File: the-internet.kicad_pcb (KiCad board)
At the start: 2 copper layers, 88 x 40 mm, 12 parts, among them J1 POWER, J2 LOLIN-C3-MINI (L), J3 LOLIN-C3-MINI (R), Q1 KSC1815YTA

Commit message: Maximise space for meme text
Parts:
- turned LS1 to 45 degrees
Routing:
- net +3.3V: track 64.6 -> 70.5 mm
- net Net-(Q1-C): track 68.3 -> 71.3 mm
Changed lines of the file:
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@@
 	(footprint "the-internet:PS1720P02"
 		(layer "F.Cu")
-		(at 77.47 45.4)
+		(at 77.47 45.4 45)
 		(property "Reference" "LS1"
-			(at 0 -9.652 0)
+			(at 0 -9.652 45)
 			(unlocked yes)
 			(layer "F.SilkS")
@@
 		)
 		(property "Value" "PS1720P02"
-			(at 0 1 0)
+			(at 0 1 45)
 			(unlocked yes)
 			(layer "F.Fab")
@@
 		)
 		(property "Datasheet" "https://product.tdk.com/en/system/files/dam/doc/product/sw_piezo/sw_piezo/piezo-buzzer/catalog/piezoelectronic_buzzer_ps_en.pdf"
-			(at 0 0 0)
+			(at 0 0 45)
 			(unlocked yes)
 			(layer "F.Fab")
@@
 		)
 		(property "Description" "Crystal speaker/transducer"
-			(at 0 0 0)
+			(at 0 0 45)
 			(unlocked yes)
 			(layer "F.Fab")
@@
 		(fp_circle
 			(center 0 0)
-			(end 8.5 0)
+			(end 8.500001 0)
 			(stroke
 				(width 0.1)
@@
 		)
 		(fp_text user "${REFERENCE}"
-			(at 0 2.5 0)
+			(at 0 2.5 45)
 			(unlocked yes)
 			(layer "F.Fab")
@@
 		)
 		(pad "1" thru_hole circle
-			(at -5 0)
+			(at -5 0 45)
 			(size 1.4 1.4)
 			(drill 0.9)
@@
 		)
 		(pad "2" thru_hole circle
-			(at 5 0)
+			(at 5 0 45)
 			(size 1.4 1.4)
 			(drill 0.9)
@@
 	)
 	(gr_text "2018\n2019\n2020\n2021\n2022\n2023\n2024"
-		(at 60.96 38.1 0)
+		(at 63.754 38.1 0)
 		(layer "B.SilkS")
 		(effects
@@
 	)
 	(gr_text "September X, 1993\nDas gibt's doch gar nicht\n{dblquote}Toddler with Diaper{dblquote} Model #5653\nIt's over 9000!\nHampster Dance\nAll your base are belong to us\nUwU\nYou're The Man Now, Dog!\nEvery time you masturbate... God kills a kitten\nBadger Badger Badger\nYou Wouldn't Steal a Car\nChuck Norris can divide by zero\nDownfall\nNever Gonna Give You Up\nLoss     | || || |_\nAll Star (Shrek)\nPogChamp\nNyan Cat\nIs This a Pigeon?\nDoge     wow   very silkscreen\nPress F to pay respects\nBe like Bill\nThis is fine\nDistracted boyfriend"
-		(at 105.537 26.289 0)
+		(at 105.664 26.289 0)
 		(layer "B.SilkS")
 		(effects
@@
 	)
 	(gr_text "Galaxy Brain\nSir, this is a Wendy's\nSoyjaks vs. Chads\namogus (sus)\nGirl Explaining\nYou Like Kissing Boys Don't You\nA Circle?? In the Triangle Factory??"
-		(at 60.452 38.1 0)
+		(at 63.246 38.1 0)
 		(layer "B.SilkS")
 		(effects
@@
 			(keep_text_aligned yes)
 		)
-		(gr_text "88 mm"
+		(gr_text "3464.5669 mils"
 			(at 69.4 69.97 0)
 			(layer "Cmts.User")
@@
 			(keep_text_aligned yes)
 		)
-		(gr_text "5.08"
+		(gr_text "200"
 			(at 19.17 62.865 90)
 			(layer "Cmts.User")
@@
 	)
 	(segment
+		(start 66.675 33.02)
+		(end 61.595 33.02)
+		(width 0.2)
+		(layer "B.Cu")
+		(net 2)
+	)
+	(segment
+		(start 68.58 34.925)
+		(end 66.675 33.02)
+		(width 0.2)
+		(layer "B.Cu")
+		(net 2)
+	)
+	(segment
+		(start 72.430534 48.935534)
+		(end 68.58 45.085)
+		(width 0.2)
+		(layer "B.Cu")
+		(net 2)
+	)
+	(segment
+		(start 73.934466 48.935534)
+		(end 72.430534 48.935534)
+		(width 0.2)
+		(layer "B.Cu")
+		(net 2)
+	)
+	(segment
+		(start 68.58 45.085)
+		(end 68.58 34.925)
+		(width 0.2)
+		(layer "B.Cu")
+		(net 2)
+	)
+	(segment
 		(start 59.055 30.48)
 		(end 54.61 30.48)
@@
 	)
 	(segment
-		(start 68.895 45.4)
-		(end 66.04 42.545)
+		(start 61.595 33.02)
+		(end 59.055 30.48)
 		(width 0.2)
 		(layer "B.Cu")
@@
 	)
 	(segment
-		(start 66.04 37.465)
-		(end 59.055 30.48)
-		(width 0.2)
-		(layer "B.Cu")
-		(net 2)
-	)
-	(segment
-		(start 66.04 42.545)
-		(end 66.04 37.465)
-		(width 0.2)
-		(layer "B.Cu")
-		(net 2)
-	)
-	(segment
-		(start 72.47 45.4)
-		(end 68.895 45.4)
-		(width 0.2)
-		(layer "B.Cu")
-		(net 2)
-	)
-	(segment
 		(start 63.405 59.055)
 		(end 63.405 57.055)
@@
 	)
 	(segment
-		(start 82.47 45.4)
-		(end 80.965 45.4)
+		(start 77.47 43.815)
+		(end 79.420534 41.864466)
 		(width 0.2)
 		(layer "B.Cu")
@@
 	)
 	(segment
-		(start 77.47 48.895)
-		(end 77.47 59.055)
+		(start 77.47 59.055)
+		(end 77.47 43.815)
 		(width 0.2)
 		(layer "B.Cu")
@@
 	)
 	(segment
-		(start 80.965 45.4)
-		(end 77.47 48.895)
+		(start 79.420534 41.864466)
+		(end 81.005534 41.864466)
 		(width 0.2)
 		(layer "B.Cu")

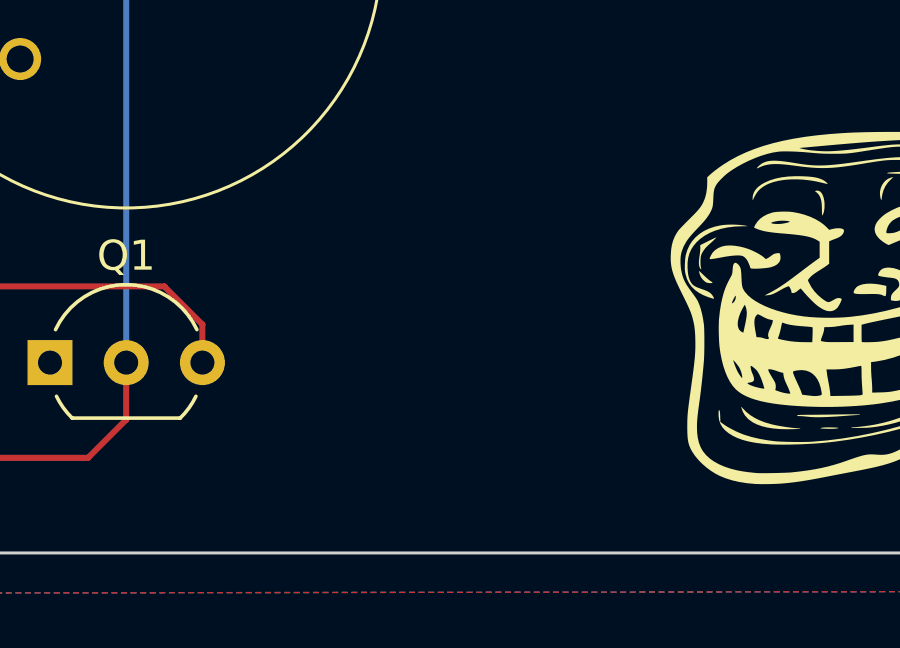
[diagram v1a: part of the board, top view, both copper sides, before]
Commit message: Add square hole game
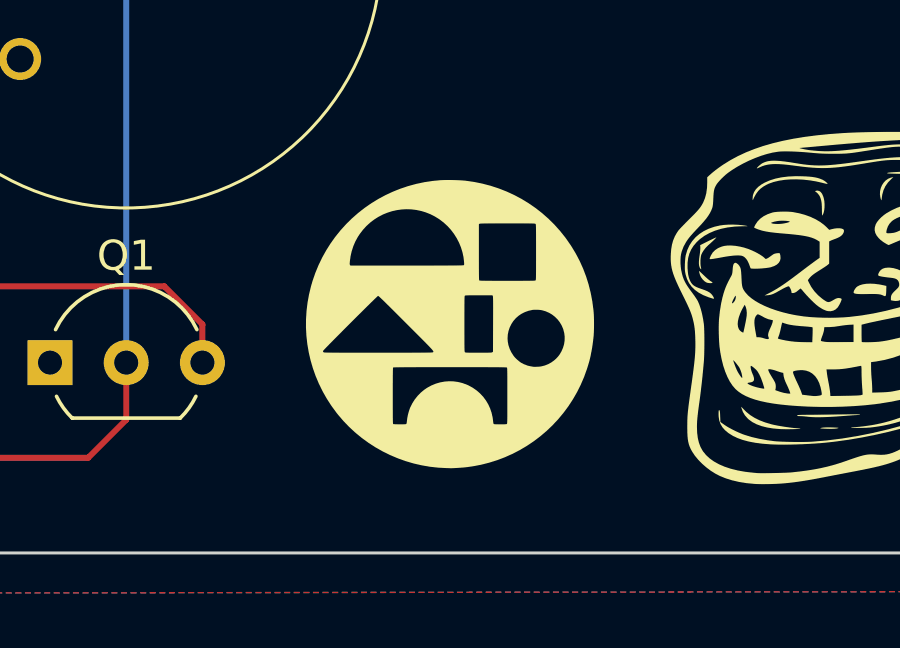
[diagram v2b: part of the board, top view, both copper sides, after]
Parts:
- added SQUARE_HOLE: LOGO, LOGO, F.Cu at (88.3, 57.8)

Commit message: Add monkey
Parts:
- added MONKEY: LOGO, LOGO, F.Cu at (77.5, 32.1)

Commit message: Add among us character
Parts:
- added SUS: LOGO, LOGO, F.Cu at (31.5, 30.5)
- moved CAKE 4.95 mm to (38.6, 30.5)
